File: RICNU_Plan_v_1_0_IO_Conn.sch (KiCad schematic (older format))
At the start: 5 parts, among them J5 MOLEX-PC20

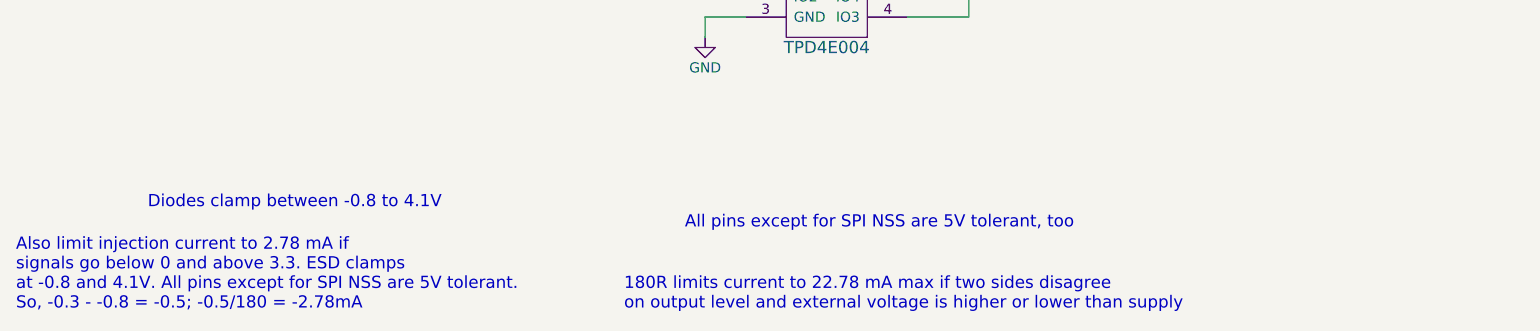
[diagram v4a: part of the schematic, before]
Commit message: Deleting PDFs
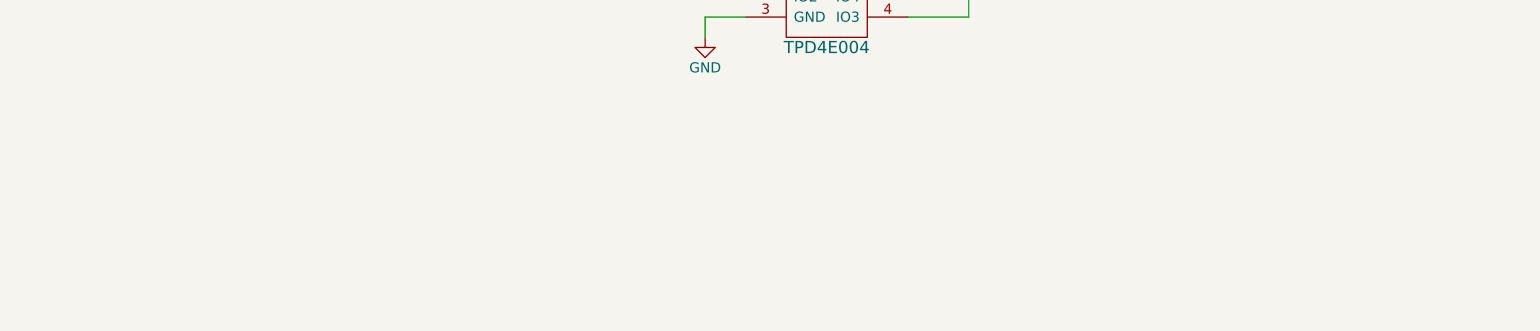
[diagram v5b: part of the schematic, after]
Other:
- note removed: "180R limits current to 22.78 mA max if two sides disagree\non output level and external voltage is higher or lower than supply"
- note removed: "All pins except for SPI NSS are 5V tolerant, too"
- note removed: "Also limit injection current to 2.78 mA if \nsignals go below 0 and above 3.3. ESD clamps \nat -0.8 and 4.1V. All pins except for SPI NSS are 5V tolerant.\nSo, -0.3 - -0.8 = -0.5; -0.5/180 = -2.78mA"
- note removed: "Diodes clamp between -0.8 to 4.1V"
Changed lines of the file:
@@
 	1    0    0    -1
 $EndComp
-Text Notes 3800 7400 0    60   ~ 0
-180R limits current to 22.78 mA max if two sides disagree\non output level and external voltage is higher or lower than supply
-Text Notes 1450 6900 0    60   ~ 0
-Diodes clamp between -0.8 to 4.1V
-Text Notes 800  7400 0    60   ~ 0
-Also limit injection current to 2.78 mA if \nsignals go below 0 and above 3.3. ESD clamps \nat -0.8 and 4.1V. All pins except for SPI NSS are 5V tolerant.\nSo, -0.3 - -0.8 = -0.5; -0.5/180 = -2.78mA
-Text Notes 4100 7000 0    60   ~ 0
-All pins except for SPI NSS are 5V tolerant, too
 Wire Wire Line
 	3650 5250 5600 5250
